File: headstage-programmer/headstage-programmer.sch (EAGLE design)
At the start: 25 parts, among them Q1 DMP3056L, U1 TPS61202

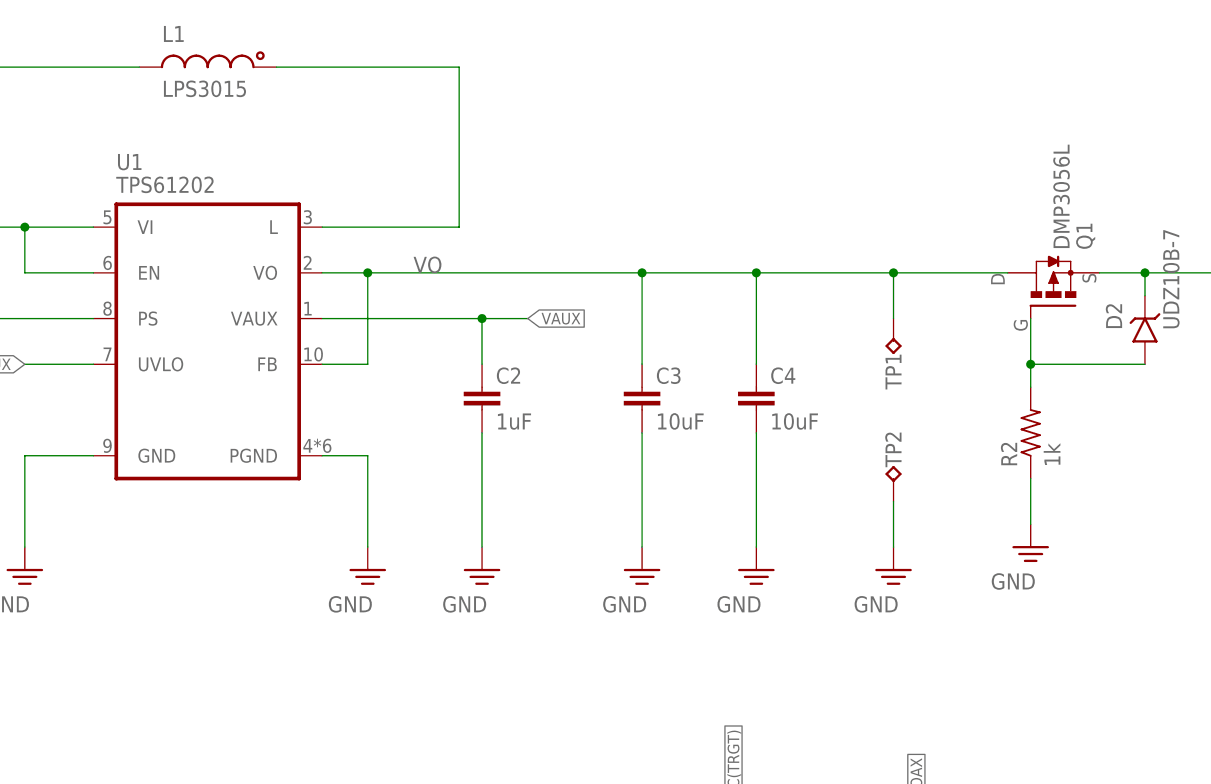
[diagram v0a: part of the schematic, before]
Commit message: Minor changes to headstage-programmer
- Made inductor part number specify actual inductance rather than just
series
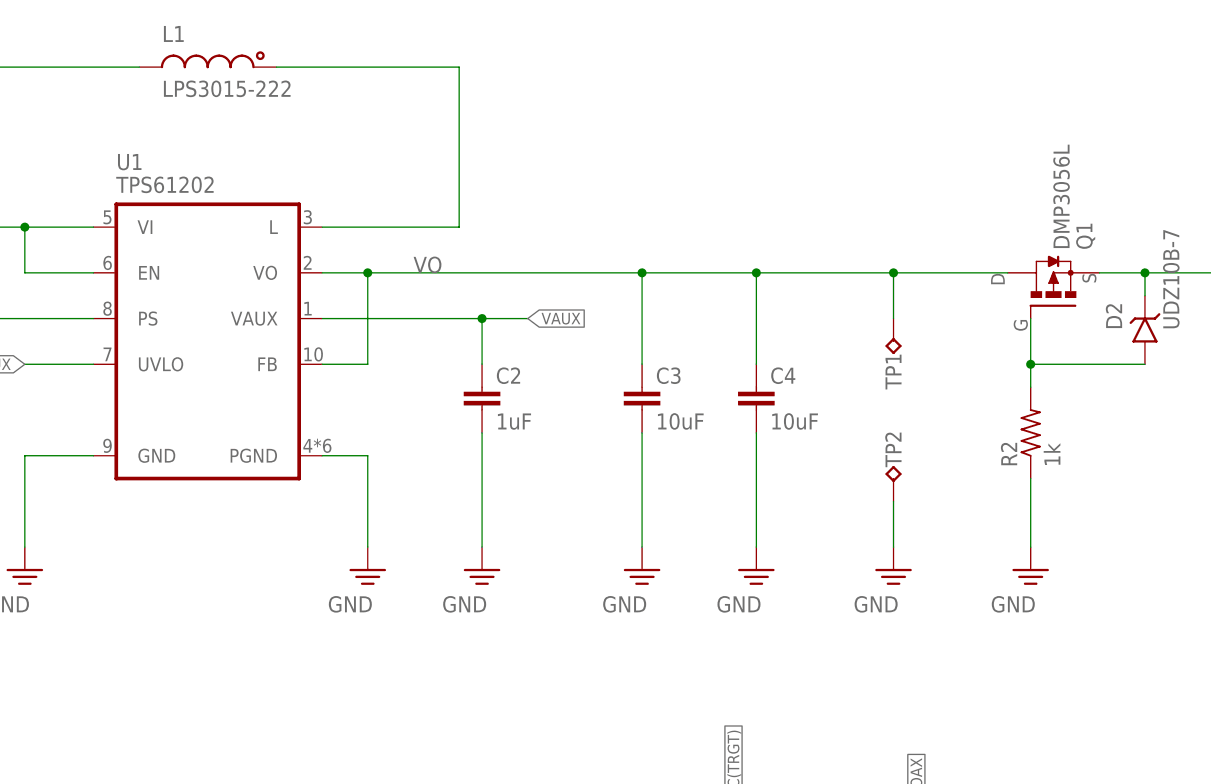
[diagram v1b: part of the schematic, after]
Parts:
- L1: value LPS3015 -> LPS3015-222
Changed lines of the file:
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@@
 <part name="TMS" library="jonnew" deviceset="TP" device="_S500-6350-P2"/>
 <part name="U1" library="jonnew" deviceset="TPS61200" device="" value="TPS61202"/>
-<part name="L1" library="jonnew" deviceset="L" device="_LPS3015" value="LPS3015"/>
+<part name="L1" library="jonnew" deviceset="L" device="_LPS3015" value="LPS3015-222"/>
 <part name="C1" library="jonnew" deviceset="C" device="_0805" value="10uF"/>
 <part name="C3" library="jonnew" deviceset="C" device="_0805" value="10uF"/>
@@
 <attribute name="PARTNO" x="210.82" y="144.78" size="1.778" layer="96" rot="MR90" display="off"/>
 </instance>
-<instance part="SUPPLY27" gate="PE" x="208.28" y="114.3"/>
+<instance part="SUPPLY27" gate="PE" x="208.28" y="111.76"/>
 <instance part="R3" gate="R" x="195.58" y="73.66" rot="R90"/>
 <instance part="D3" gate="G$1" x="195.58" y="60.96"/>
@@
 <pinref part="R2" gate="R" pin="1"/>
 <pinref part="SUPPLY27" gate="PE" pin="GND"/>
-<wire x1="208.28" y1="121.92" x2="208.28" y2="116.84" width="0.1524" layer="91"/>
-</segment>
-<segment>
+<wire x1="208.28" y1="121.92" x2="208.28" y2="114.3" width="0.1524" layer="91"/>
+</segment>
+<segment>

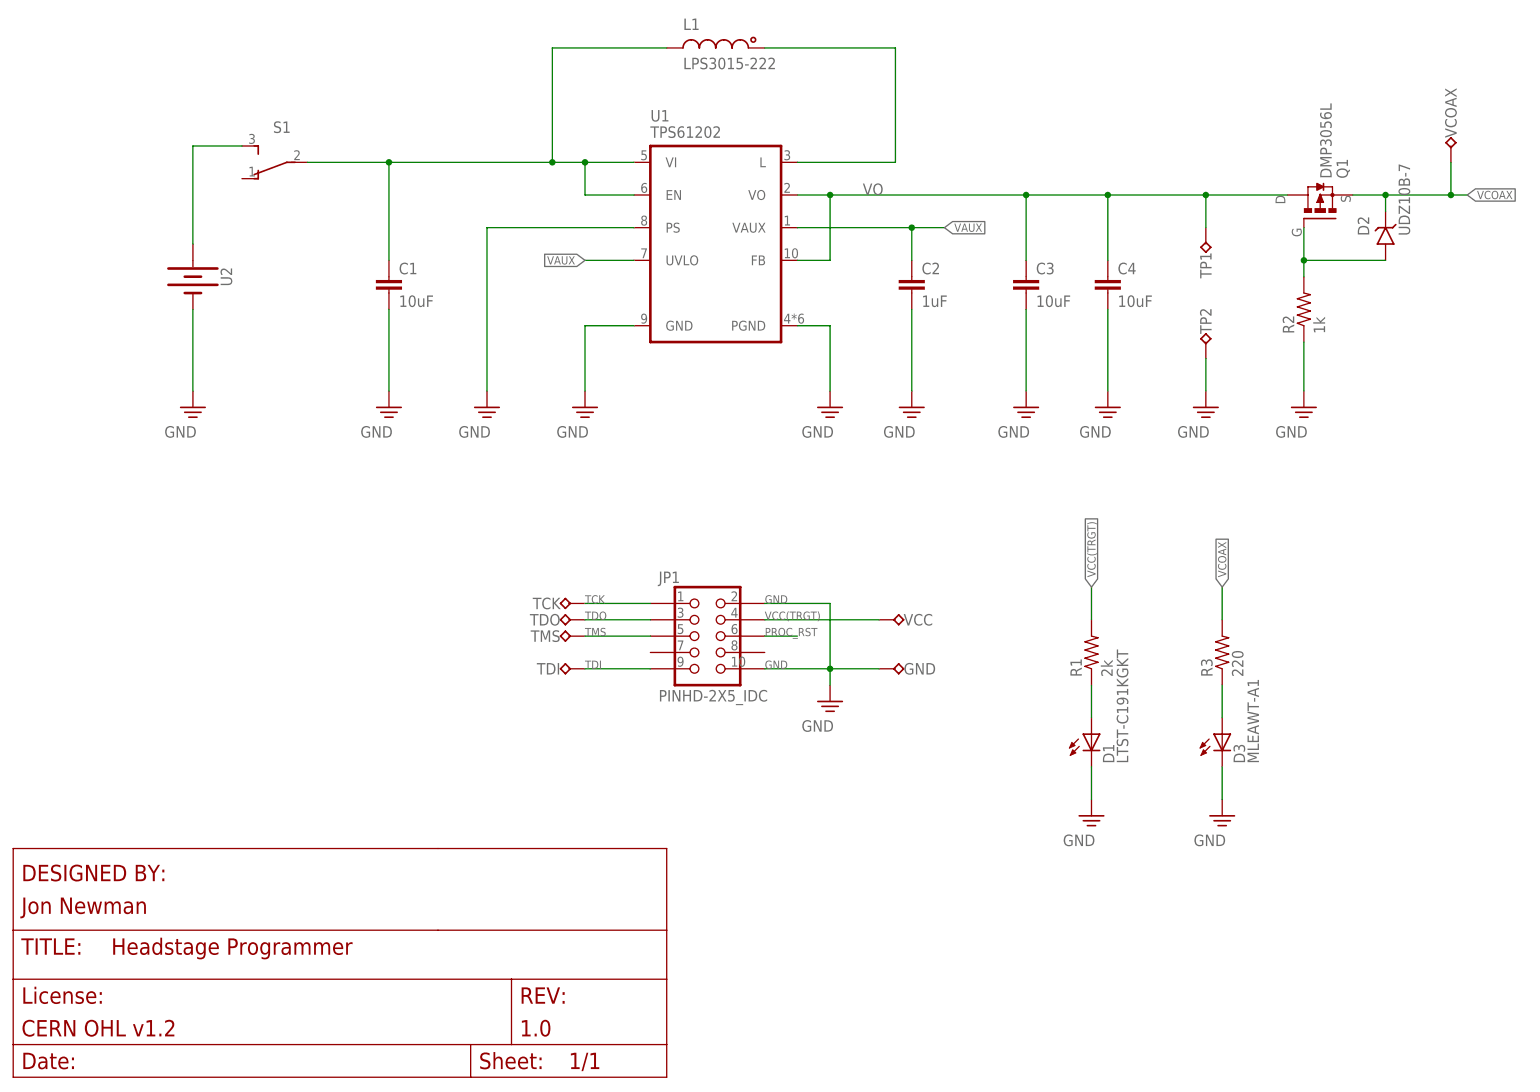
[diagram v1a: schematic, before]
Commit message: Fixes to headstage programmer
- Added switch to turn off bottom LED
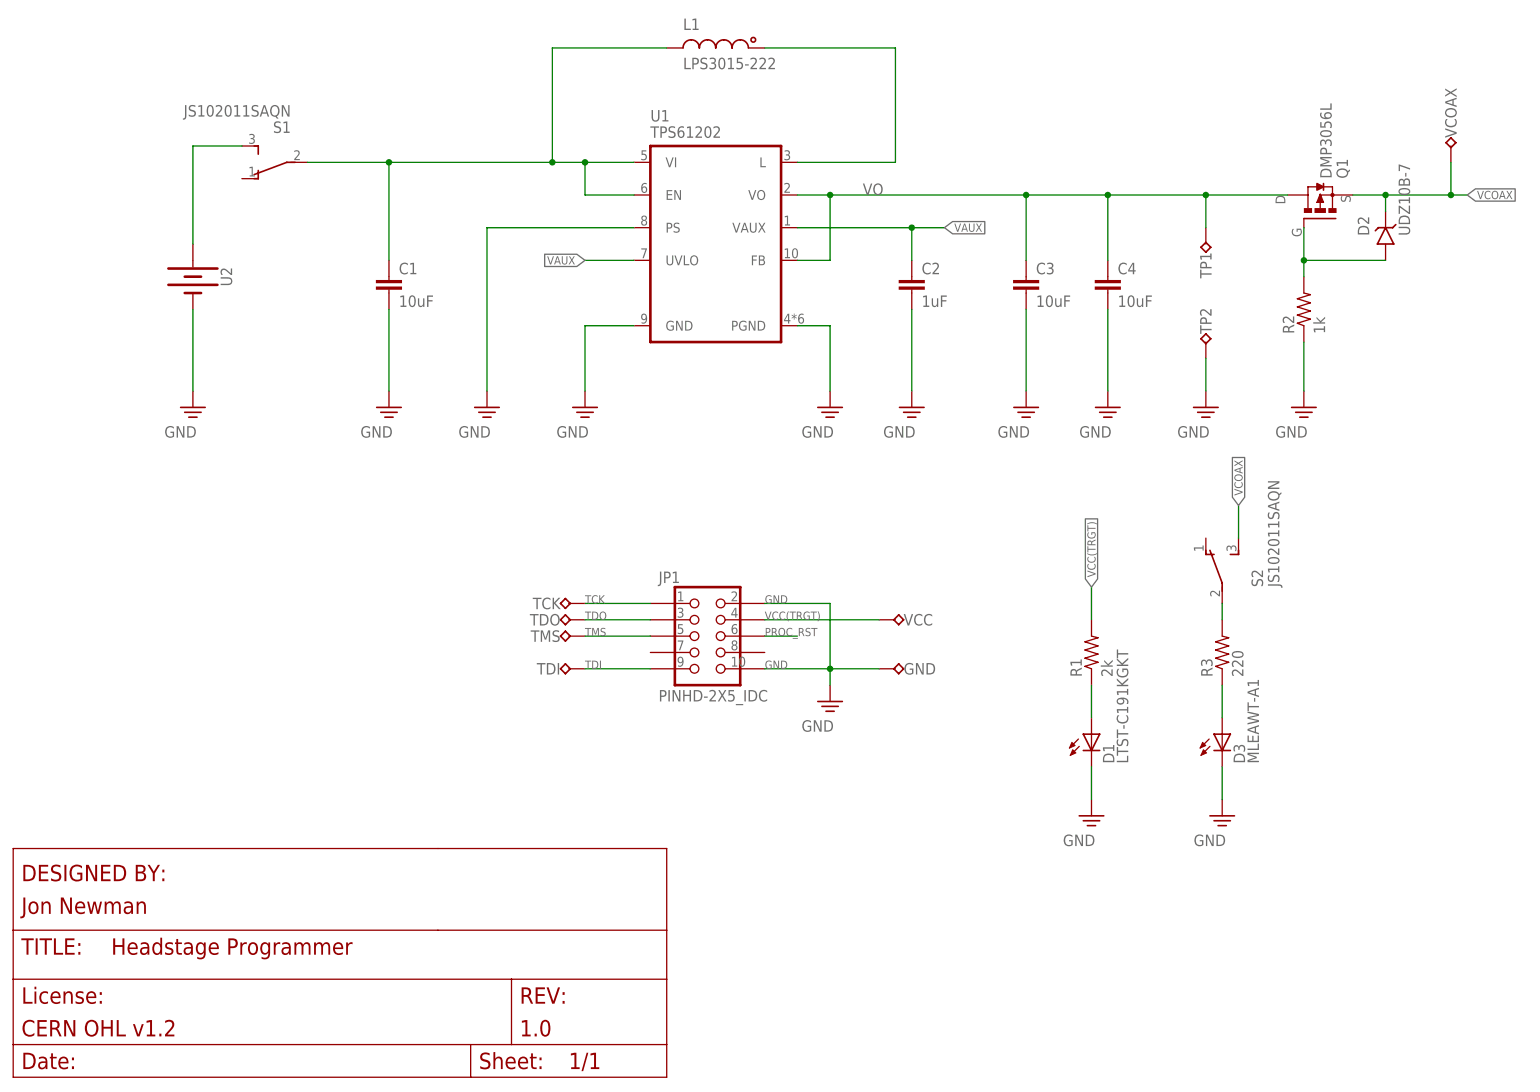
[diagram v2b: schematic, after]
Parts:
- added S2: JS102011SAQN, jonnew:SPDT_JS
- S1: value (none) -> JS102011SAQN
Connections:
- new net N$6: R3.2, S2.2
- net VCOAX: now also S2.3; no longer R3.2
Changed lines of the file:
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@@
 <part name="D3" library="jonnew" deviceset="LED" device="_MLE-HS-CAT" value="MLEAWT-A1"/>
 <part name="SUPPLY12" library="jonnew" deviceset="GND" device=""/>
-<part name="S1" library="jonnew" deviceset="SPDT" device="_JS"/>
+<part name="S1" library="jonnew" deviceset="SPDT" device="_JS" value="JS102011SAQN"/>
+<part name="S2" library="jonnew" deviceset="SPDT" device="_JS" value="JS102011SAQN"/>
 </parts>
 <sheets>
@@
 <instance part="SUPPLY12" gate="PE" x="195.58" y="48.26"/>
 <instance part="S1" gate="G$1" x="50.8" y="149.86" rot="R180"/>
+<instance part="S2" gate="G$1" x="195.58" y="83.82" rot="R90"/>
 </instances>
 <busses>
@@
 </segment>
 <segment>
-<pinref part="R3" gate="R" pin="2"/>
-<wire x1="195.58" y1="83.82" x2="195.58" y2="78.74" width="0.1524" layer="91"/>
-<label x="195.58" y="83.82" size="1.27" layer="95" rot="R90" xref="yes"/>
+<wire x1="198.12" y1="96.52" x2="198.12" y2="91.44" width="0.1524" layer="91"/>
+<label x="198.12" y="96.52" size="1.27" layer="95" rot="R90" xref="yes"/>
+<pinref part="S2" gate="G$1" pin="3"/>
 </segment>
 </net>
@@
 </segment>
 </net>
+<net name="N$6" class="0">
+<segment>
+<pinref part="S2" gate="G$1" pin="2"/>
+<pinref part="R3" gate="R" pin="2"/>
+<wire x1="195.58" y1="81.28" x2="195.58" y2="78.74" width="0.1524" layer="91"/>
+</segment>
+</net>

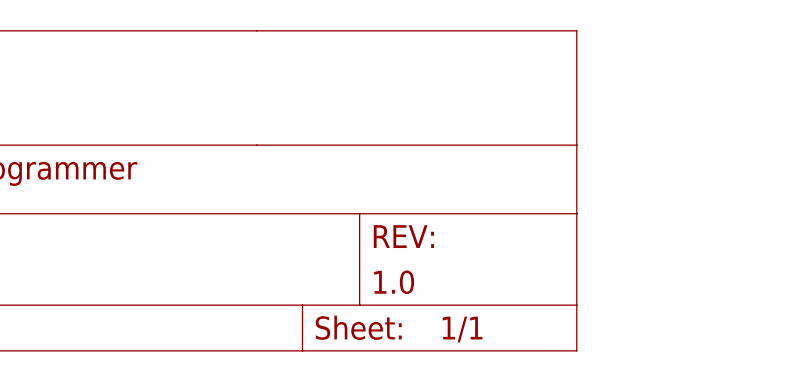
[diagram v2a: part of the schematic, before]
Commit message: Lots of small fixes and cleanup
- Taking care of little issues that have been bothering me
- Dediated serdes interface board moved to deprecated
- Non-serialized headstage moved to deprecated
- Deleted top-level datasheets directory which does not really
apply to anything anymore
- Added pdfs versions of board schematics so that eagle is not
needed to see them.
- Small fixes to test-boards: High power LEDs moved to bottom to prevent
blinding ppl. Silkscreen improved. License updated. Etc. Gerbers
updated.
- Removed random deprecated design files where I found them.
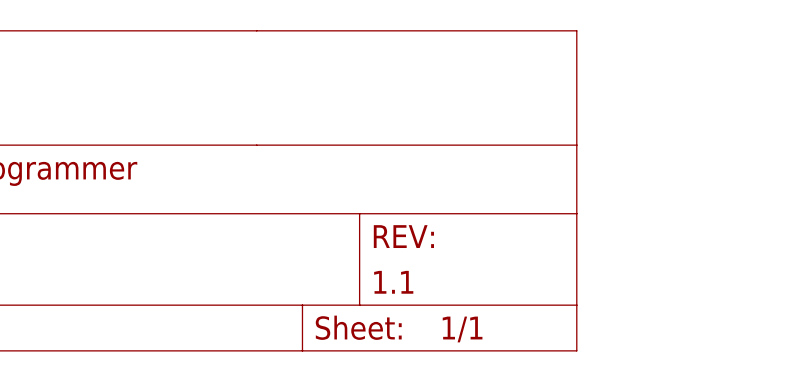
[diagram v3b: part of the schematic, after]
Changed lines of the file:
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@@
 <attribute name="DESIGN_NAME" value="Headstage Programmer"/>
 <attribute name="LICENSE" value="CERN OHL v1.2"/>
-<attribute name="REVISION" value="1.0"/>
+<attribute name="REVISION" value="1.1"/>
 </attributes>
 <variantdefs>
